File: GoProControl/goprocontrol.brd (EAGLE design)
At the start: 54.2 x 51.8 mm, 19 parts, among them Q1 IRLML6344

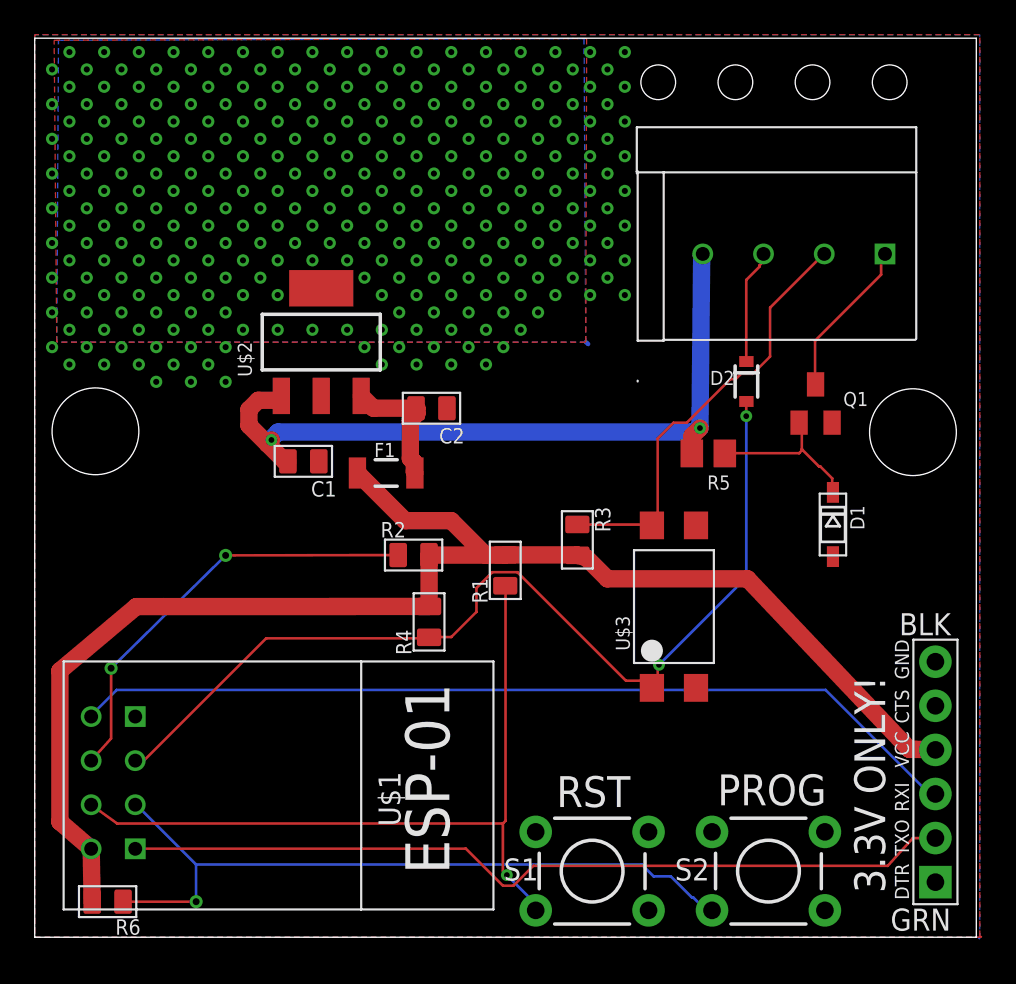
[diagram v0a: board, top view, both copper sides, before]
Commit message: Update PCB to v0.5
- Switch to using more common 5V FTDI (VCC & signal)
- Use Schottky diodes to protect reverse polarity and
  to make sure we don't send 12V onto the FTDI VCC line
- Add 1uF cap to VCC on ESP8266 to stabilize things

Still would be a good idea to protect against the FTDI
cable being inserted backwards and putting 5V onto RXD
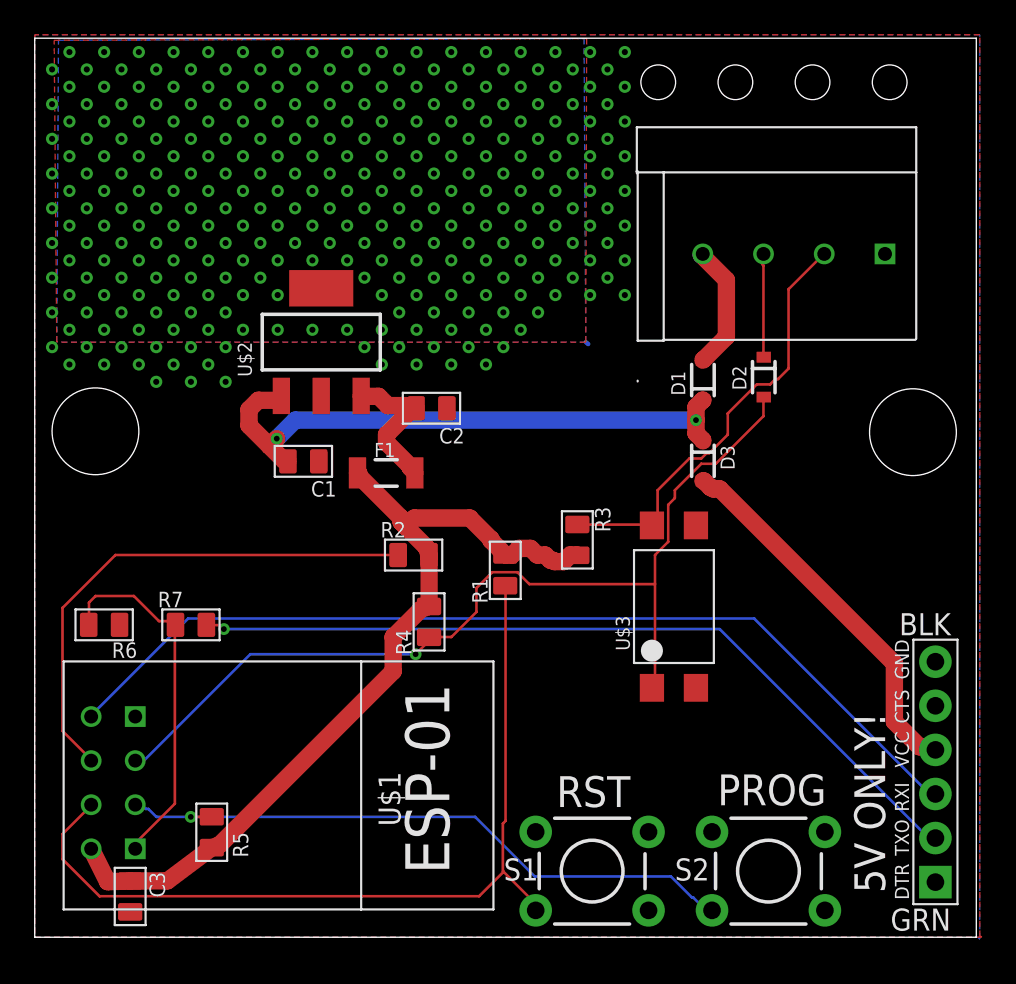
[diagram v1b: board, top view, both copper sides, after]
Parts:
- removed Q1: IRLML6344, synfinatic:SOT23
- added C3: 1uf, Seeed-OPL-Capacitor:C0805
- added D3: B5817WS, synfinatic:SOD-323
- added R7: 22K, Seeed-OPL-Resistor:R0805
- D1: value 10V Z -> B5817WS; device adafruit:SOD-123 -> synfinatic:SOD-323
- R5: value 13.3k -> 10K; device resistor:M0805 -> Seeed-OPL-Resistor:R0805
- moved R5 36.0 mm to (10.2, 6.05), turned to 0 degrees
- moved R6 16.0 mm to (4.00, 18.0)
- moved D1 11.2 mm to (38.5, 32.1), turned to 90 degrees
- moved D2 1.03 mm to (42.0, 32.3)
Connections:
- removed net CTS: JP1.P$5
- removed net DTR: JP1.P$1
- removed net GND_MAIN: Q1.3, U$4.P$1
- removed net N$17: D1.C, Q1.1, R5.1
- new net N$4: D3.A, JP1.P$4
- new net N$6: D1.A, U$4.P$4
- new net N$8: JP1.P$2, R7.2
- net +12V: now also D1.C, D3.C; no longer R5.2, U$4.P$4
- net 3.3V: now also C3.2, R5.2; no longer JP1.P$4, R6.2
- net GND: now also C3.1, R6.1, U$4.P$1; no longer D1.A, Q1.2
- net GPIO0: now also R5.1; no longer R6.1
- net TXD: now also R6.2, R7.1; no longer JP1.P$2
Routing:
- net N$8: track 0.00 -> 47.1 mm, vias 0 -> 1
- net 3.3V: track 82.7 -> 49.2 mm
- net TXD: track 48.1 -> 21.0 mm
- net N$4: track 0.00 -> 21.8 mm
- net N$17: track 9.43 -> 0.00 mm
- net +12V: track 43.3 -> 34.1 mm
- net GND_MAIN: track 9.23 -> 0.00 mm
- net N$6: track 0.00 -> 7.61 mm
- net N$3: track 43.6 -> 50.3 mm, vias 1 -> 0
- net GPIO0: track 42.1 -> 37.0 mm
- net N$1: track 25.0 -> 30.1 mm, vias 2 -> 0
- net RXD: track 51.8 -> 55.2 mm
- net GPIO2: track 56.6 -> 55.5 mm, vias 2 -> 1
- net 3.3-UNPRO: track 7.50 -> 8.36 mm
- net INPUT: track 6.61 -> 6.02 mm
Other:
- board text added: "5V ONLY!"
- board text added: "GoProControl v0.5 http://synfin.net/goprocontrol"
- board text removed: "3.3V ONLY!"
- board text removed: "GoProControl v0.4 http://synfin.net/goprocontrol"

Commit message: Update PCB to v0.6
- Replace LDO with a switching module
- Update readme file
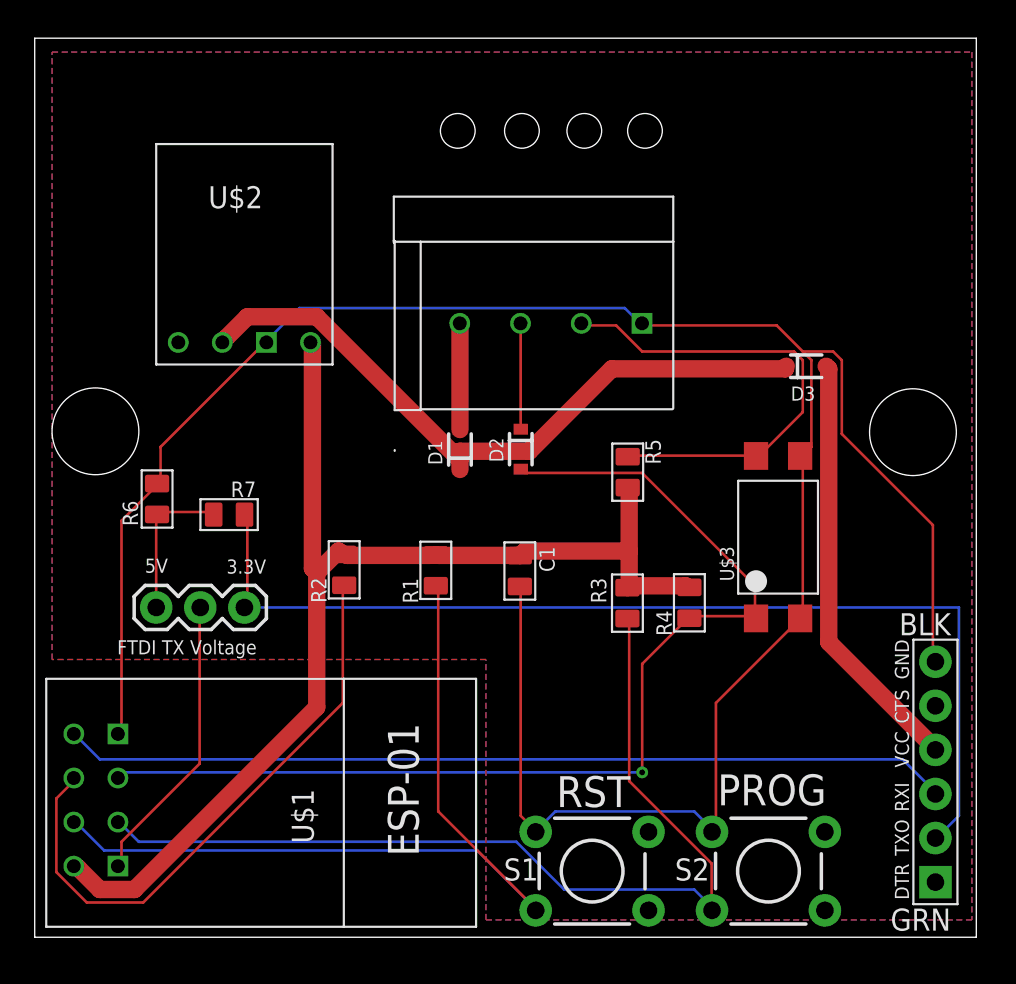
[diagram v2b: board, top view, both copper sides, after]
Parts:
- removed C2, C3: 1uf, Seeed-OPL-Capacitor:C0805
- removed F1: PTCSMD-W, SparkFun-PowerIC:PTC-1206-WIDE
- added JP2: (no value), SparkFun-Connectors:1X03
- U$2: value MCP1825SOT-223-3 -> POLOLU-D24V5F3; device synfinatic:SOT-223 -> synfinatic:POLOLU-D24V5FX
- moved R5 31.7 mm to (34.2, 26.8)
- moved R4 15.0 mm to (37.7, 19.3)
- moved D2 14.6 mm to (28.0, 28.1)
- moved D1 14.6 mm to (24.5, 28.1)
- moved U$4 14.6 mm to (35.0, 35.4)
- moved C1 14.0 mm to (27.9, 21.1), turned to 180 degrees
- moved U$2 9.60 mm to (7.00, 33.0)
- moved D3 8.07 mm to (44.5, 32.9), turned to 0 degrees
- moved R6 7.87 mm to (7.05, 25.2), turned to 0 degrees
- moved U$3 7.21 mm to (42.8, 23.1)
- moved R7 6.72 mm to (11.2, 24.4)
- moved R3 4.65 mm to (34.1, 19.2), turned to 180 degrees
- moved R2 4.09 mm to (17.8, 21.2), turned to 180 degrees
- moved R1 4.00 mm to (23.1, 21.1)
- moved U$1 1.41 mm to (10.4, 7.89)
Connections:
- removed net 3.3-UNPRO: C2.2, F1.1, U$2.3
- removed net N$8: JP1.P$2, R7.2
- new net 3.3V-TX: JP1.P$2, JP2.3, R7.2
- new net 5V-TX: JP2.1, R6.2, R7.1
- net +12V: now also U$2.VIN; no longer C1.2, U$2.1
- net 3.3V: now also C1.2, U$2.VOUT; no longer C3.2, F1.2
- net GND: now also U$2.GND; no longer C2.1, C3.1, U$2.2, U$2.4
- net GPIO0: now also R3.1; no longer R5.1
- net OUTPUT: now also R5.1; no longer R3.1
- net TXD: now also JP2.2; no longer R6.2, R7.1
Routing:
- net GND: track 0.18 -> 137.3 mm, vias 299 -> 0
- net 3.3V-TX: track 0.00 -> 60.7 mm
- net N$8: track 47.1 -> 0.00 mm, vias 1 -> 0
- net 3.3V: track 49.2 -> 68.1 mm
- net GPIO0: track 37.0 -> 55.2 mm, vias 1 -> 0
- net 5V-TX: track 0.00 -> 8.78 mm
- net 3.3-UNPRO: track 8.36 -> 0.00 mm
- net GPIO2: track 55.5 -> 62.4 mm
- net +12V: track 34.1 -> 39.5 mm, vias 2 -> 0
- net N$1: track 30.1 -> 34.7 mm
- net RXD: track 55.2 -> 51.1 mm
- net TXD: track 21.0 -> 16.9 mm
- net N$4: track 21.8 -> 24.7 mm
- net OUTPUT: track 25.1 -> 27.8 mm
- net N$6: track 7.61 -> 6.12 mm
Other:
- board text added: "3.3V"
- board text added: "5V"
- board text added: "FTDI TX Voltage"
- board text added: "GoProControl v0.6 http://synfin.net/goprocontrol"
- board text added: "U$2"
- board text removed: "5V ONLY!"
- board text removed: "GoProControl v0.5 http://synfin.net/goprocontrol"

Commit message: Update board to v0.7
- Fixes FTDI RX/TX reversal
- Fixes GPIO2 pullup
- Rotated termblock
- Still needs to fix term block part to match
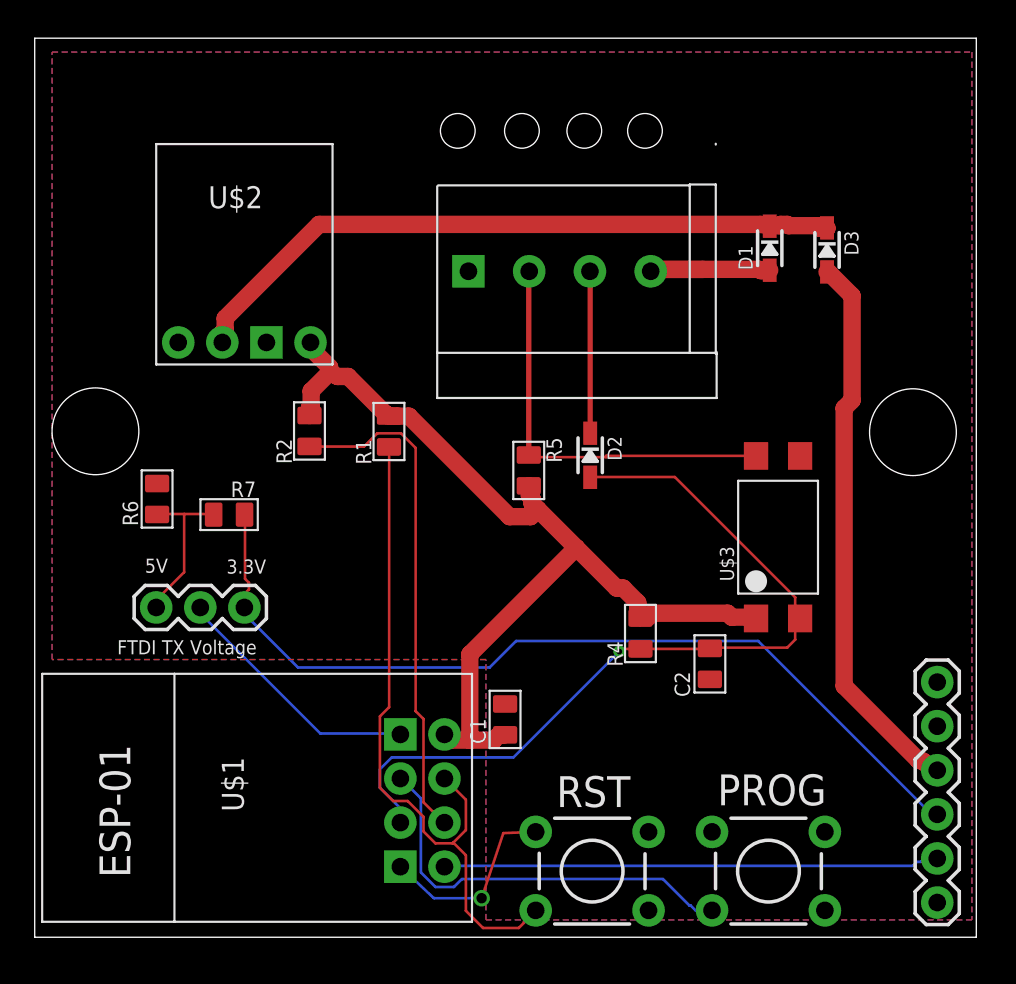
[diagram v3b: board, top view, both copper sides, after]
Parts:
- removed R3: 10K, Seeed-OPL-Resistor:R0805
- added C2: .01uf, Seeed-OPL-Capacitor:C0805
- JP1: value FTDI_DEVICE -> FTDI_BASICPTH; device SparkFun-Connectors:FTDI_DEVICE_SIDE -> SparkFun-Connectors:FTDI_BASIC
- R1, R2, R5: value 10K -> 1k
- R4: value 1K -> 1k
- moved D1 21.3 mm to (42.4, 39.7), turned to 270 degrees
- moved U$4 10.4 mm to (25.0, 38.4), turned to 0 degrees
- moved C1 8.59 mm to (27.1, 12.6), turned to 0 degrees
- moved R1 8.44 mm to (20.4, 29.1)
- moved R2 8.25 mm to (15.8, 29.2)
- moved JP1 7.53 mm to (52.0, 2.00)
- moved D3 6.81 mm to (45.6, 39.6), turned to 270 degrees
- moved R5 5.70 mm to (28.5, 26.9)
- moved U$1 5.00 mm to (15.4, 7.89), turned to 90 degrees
- moved D2 4.02 mm to (32.0, 27.8)
- moved R4 3.33 mm to (34.9, 17.5)
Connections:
- net +12V: now also D1.C1, D3.C1; no longer D1.C, D3.C
- net 3.3V: now also U$3.1; no longer R3.2
- net 3.3V-TX: now also JP1.TXO; no longer JP1.P$2
- net GND: now also C2.1, JP1.GND; no longer JP1.P$6, U$3.2
- net GPIO0: no longer R3.1
- net GPIO2: now also C2.2, D2.A1, U$3.2; no longer D2.A, U$3.1
- net INPUT: now also D2.C1; no longer D2.C
- net N$4: now also D3.A1, JP1.VCC; no longer D3.A, JP1.P$4
- net N$6: now also D1.A1; no longer D1.A
- net RXD: now also JP1.RXI; no longer JP1.P$3
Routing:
- net GND: track 137.3 -> 11.2 mm, vias 0 -> 1
- net GPIO0: track 55.2 -> 24.0 mm
- net RXD: track 51.1 -> 28.6 mm
- net GPIO2: track 62.4 -> 48.0 mm
- net 3.3V: track 68.1 -> 55.5 mm
- net N$3: track 49.9 -> 39.6 mm
- net 3.3V-TX: track 60.7 -> 51.9 mm
- net N$4: track 24.7 -> 32.1 mm
- net N$1: track 34.7 -> 29.1 mm
- net OUTPUT: track 27.8 -> 23.8 mm
- net INPUT: track 6.10 -> 9.35 mm
- net TXD: track 16.9 -> 14.8 mm
- net N$6: track 6.12 -> 7.28 mm
- net +12V: track 39.5 -> 38.6 mm
- net 5V-TX: track 8.78 -> 9.33 mm
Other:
- board text added: "GoProControl v0.7 http://synfin.net/goprocontrol"
- board text removed: "GoProControl v0.6 http://synfin.net/goprocontrol"

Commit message: v0.8 - ordered!
- Tweaked footprints & labels
- Changed term block outline to match OST TE 3.5mm
- Added parts list
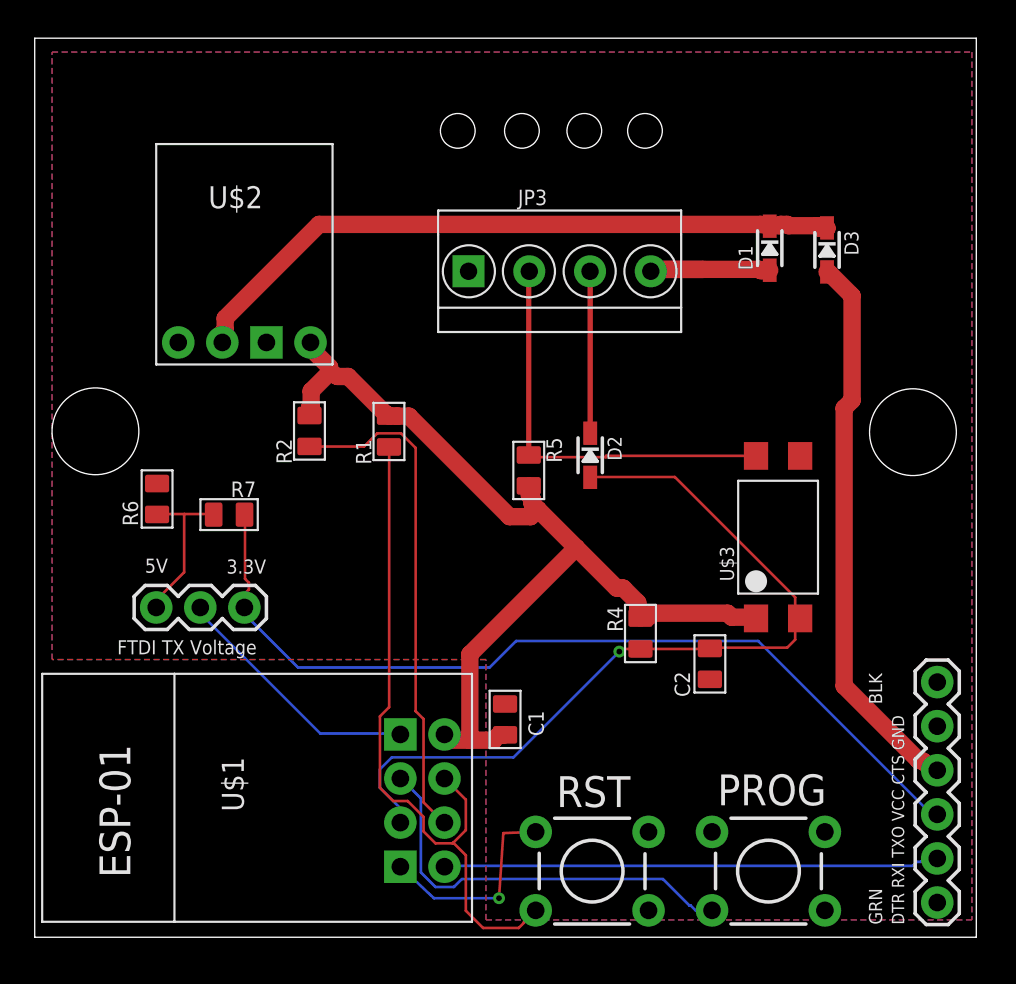
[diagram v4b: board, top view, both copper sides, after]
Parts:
- removed U$4: PTSA-1.5/4-3.5F4-3.5IP-2, synfinatic:4-3.5IP-2
- added JP3: PTSA-1.5/4-3.5FOST-TE-3.5-4P, synfinatic:TERM-4P-3.5
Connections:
- net GND: now also JP3.1; no longer U$4.P$1
- net INPUT: now also JP3.3; no longer U$4.P$3
- net N$6: now also JP3.4; no longer U$4.P$4
- net OUTPUT: now also JP3.2; no longer U$4.P$2
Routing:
- net GND: track 11.2 -> 12.0 mm
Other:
- board text added: "GoProControl v0.8 https://synfin.net/goprocontrol"
- board text removed: "GoProControl v0.7 http://synfin.net/goprocontrol"
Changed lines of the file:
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@@
 <hole x="3.5" y="29.15" drill="5"/>
 <hole x="50.6" y="29.1" drill="5"/>
-<text x="39" y="31" size="1.016" layer="26" rot="MR0">GoProControl v0.7
-http://synfin.net/goprocontrol</text>
+<text x="39" y="31" size="1.016" layer="26" rot="MR0">GoProControl v0.8
+https://synfin.net/goprocontrol</text>
 <text x="24" y="48.5" size="1.778" layer="26" rot="MR0">S/N:</text>
 <rectangle x1="1" y1="46" x2="18" y2="51" layer="26"/>
@@
 <attribute name="NAME" x="40.29" y="20.51" size="0.8128" layer="25" rot="R90"/>
 </element>
-<element name="U$4" library="synfinatic" package="4-3.5IP-2" value="PTSA-1.5/4-3.5F4-3.5IP-2" x="24.99" y="38.37"/>
+<element name="JP3" library="synfinatic" package="TERM-4P-3.5" value="PTSA-1.5/4-3.5FOST-TE-3.5-4P" x="24.99" y="38.37" smashed="yes">
+<attribute name="NAME" x="27.84" y="42.18" size="0.889" layer="25" ratio="11"/>
+</element>
 <element name="R6" library="Seeed-OPL-Resistor" package="R0805" value="10K" x="7.05" y="25.25" smashed="yes">
 <attribute name="MPN" value="RC0805FR-0710KL" x="7.05" y="25.25" size="1.778" layer="27" display="off"/>
@@
 <element name="C1" library="Seeed-OPL-Capacitor" package="C0805" value="1uf" x="27.1" y="12.55" smashed="yes">
 <attribute name="MPN" value="CC0805KKX7R8BB105" x="27.1" y="12.55" size="1.778" layer="27" display="off"/>
-<attribute name="NAME" x="25.093" y="12.605" size="0.889" layer="25" font="vector" ratio="11" rot="R270"/>
+<attribute name="NAME" x="28.443" y="13.055" size="0.889" layer="25" font="vector" ratio="11" rot="R270"/>
 </element>
 <element name="U$2" library="synfinatic" package="POLOLU-D24V5FX" value="POLOLU-D24V5F3" x="7" y="33" smashed="yes"/>
@@
 <element name="R4" library="Seeed-OPL-Resistor" package="R0805" value="1k" x="34.9" y="17.5" smashed="yes" rot="R180">
 <attribute name="MPN" value="RC0805FR-0710KL" x="34.9" y="17.5" size="1.778" layer="27" rot="R180" display="off"/>
-<attribute name="NAME" x="33.884" y="15.595" size="0.889" layer="25" font="vector" ratio="11" rot="R90"/>
+<attribute name="NAME" x="33.884" y="17.595" size="0.889" layer="25" font="vector" ratio="11" rot="R90"/>
 </element>
 </elements>
@@
 <contactref element="U$3" pad="3"/>
 <contactref element="R6" pad="1"/>
-<contactref element="U$4" pad="P$1"/>
+<contactref element="JP3" pad="1"/>
 <contactref element="C1" pad="1"/>
 <contactref element="U$2" pad="GND"/>
@@
 <contactref element="C2" pad="1"/>
 <wire x1="21.0675" y1="4.065" x2="23" y2="2.25" width="0.1524" layer="16"/>
-<wire x1="23" y1="2.25" x2="25.75" y2="2.25" width="0.1524" layer="16"/>
-<via x="25.75" y="2.25" extent="1-16" drill="0.6" shape="square"/>
-<wire x1="25.75" y1="2.25" x2="27" y2="6" width="0.1524" layer="1"/>
+<wire x1="23" y1="2.25" x2="26.75" y2="2.25" width="0.1524" layer="16"/>
+<via x="26.75" y="2.25" extent="1-16" drill="0.3302"/>
+<wire x1="26.75" y1="2.25" x2="27" y2="6" width="0.1524" layer="1"/>
 <wire x1="27" y1="6" x2="28.8638" y2="6.0706" width="0.1524" layer="1"/>
 </signal>
@@
 <signal name="INPUT">
 <contactref element="D2" pad="C1"/>
-<contactref element="U$4" pad="P$3"/>
-<wire x1="31.99" y1="38.37" x2="32.005" y2="38.37" width="0.3048" layer="1"/>
+<contactref element="JP3" pad="3"/>
+<wire x1="31.995" y1="38.37" x2="32.005" y2="38.37" width="0.3048" layer="1"/>
 <wire x1="32.005" y1="38.37" x2="32.005" y2="29.04" width="0.3048" layer="1"/>
 </signal>
@@
 <contactref element="U$3" pad="4"/>
 <contactref element="R5" pad="1"/>
-<contactref element="U$4" pad="P$2"/>
+<contactref element="JP3" pad="2"/>
 <wire x1="32.9184" y1="27.7368" x2="41.529" y2="27.7368" width="0.1524" layer="1"/>
 <wire x1="28.7274" y1="27.6606" x2="32.9184" y2="27.6606" width="0.1524" layer="1"/>
@@
 <wire x1="41.529" y1="27.7368" x2="41.56" y2="27.73" width="0.1524" layer="1"/>
 <wire x1="28.575" y1="27.813" x2="28.465" y2="27.784" width="0.1524" layer="1"/>
-<wire x1="28.49" y1="38.37" x2="28.465" y2="38.37" width="0.3048" layer="1"/>
+<wire x1="28.495" y1="38.37" x2="28.465" y2="38.37" width="0.3048" layer="1"/>
 <wire x1="28.465" y1="38.37" x2="28.465" y2="27.784" width="0.3048" layer="1"/>
 <wire x1="32.9184" y1="27.6606" x2="32.9184" y2="27.7368" width="0.1524" layer="1"/>
@@
 </signal>
 <signal name="N$6" class="1">
-<contactref element="U$4" pad="P$4"/>
+<contactref element="JP3" pad="4"/>
 <contactref element="D1" pad="A1"/>
 <wire x1="41.8338" y1="38.4048" x2="42.291" y2="38.4048" width="1" layer="1"/>
@@
 <wire x1="35.5092" y1="38.4048" x2="35.7378" y2="38.4048" width="1" layer="1"/>
 <wire x1="42.291" y1="38.4048" x2="42.35" y2="38.43" width="1" layer="1"/>
-<wire x1="35.5092" y1="38.4048" x2="35.49" y2="38.37" width="1" layer="1"/>
+<wire x1="35.5092" y1="38.4048" x2="35.495" y2="38.37" width="1" layer="1"/>
 <wire x1="38.481" y1="38.481" x2="35.49" y2="38.481" width="1.016" layer="1"/>
-<wire x1="35.49" y1="38.481" x2="35.49" y2="38.37" width="1.016" layer="1"/>
+<wire x1="35.49" y1="38.481" x2="35.495" y2="38.37" width="1.016" layer="1"/>
 </signal>
 <signal name="5V-TX">
@@
 </signal>
 </signals>
+<errors>
+</errors>
 </board>
 </drawing>
